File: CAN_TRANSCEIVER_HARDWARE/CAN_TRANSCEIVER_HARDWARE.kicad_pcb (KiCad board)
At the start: 2 copper layers, 143.7 x 76.6 mm, 112 parts, among them J101 5v_pin_terminal, J102 5V Inp, J103 SPI Remaining Pin, J104 SPI 1, J105 SPI Remaining Pin, J106 SPI 3, J107 SPI 2 Remaining Pin, J108 SPI 2, J109 SPI Remaining Pin, J110 SPI 4, J111 UART 1, J112 UART 2, J113 UART 3, J114 UART 4, J115 Screw_Terminal_01x02, J116 Screw_Terminal_01x02, J117 Screw_Terminal_01x02, J118 Screw_Terminal_01x02, J119 Screw_Terminal_01x02, J120 Screw_Terminal_01x02, J121 Screw_Terminal_01x02, J122 Screw_Terminal_01x02, SW101 SW_DIP_x04, SW102 SW_DIP_x04, U101 MCP2515-xSO, U102 MCP2515-xSO, U103 MCP2515-xSO, U104 MCP2515-xSO, U105 MCP25612FD-E/SL, U106 ATA6565-GCQW1, U107 MCP25612FD-E/SL, U108 ATA6565-GCQW1, Y101 Crystal, Y102 Crystal, Y103 Crystal, Y104 Crystal

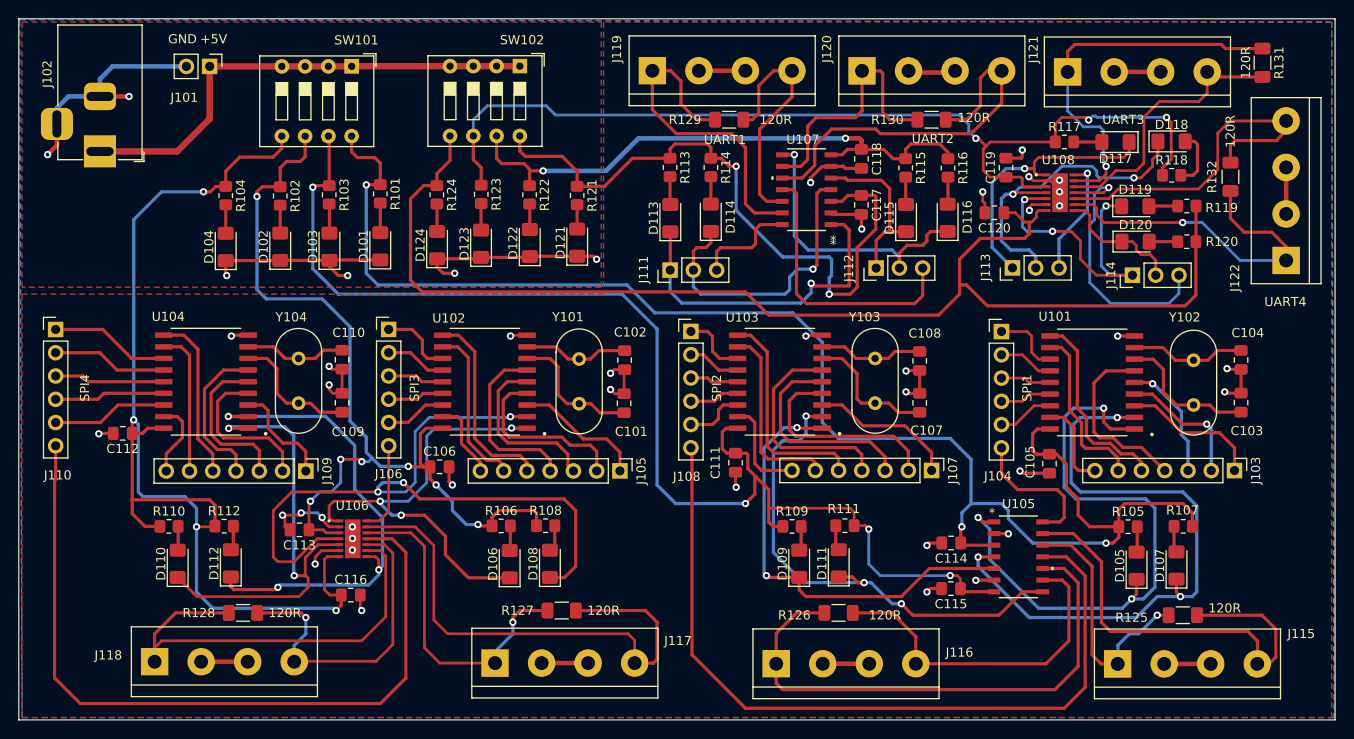
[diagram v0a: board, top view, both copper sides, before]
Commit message: Added logo in the PCB and added stackup table
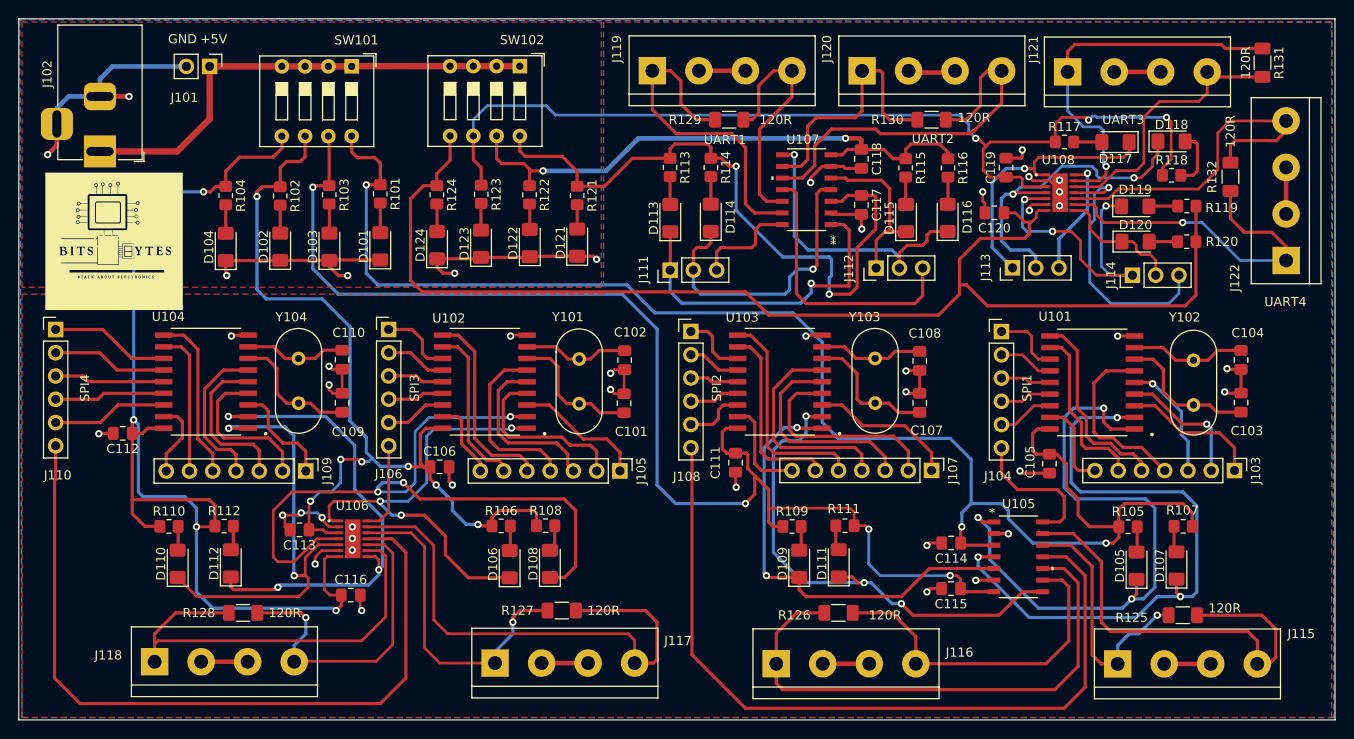
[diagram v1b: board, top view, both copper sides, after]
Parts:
- added G***: LOGO, LOGO, F.Cu at (61.1, 75.0)
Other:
- board text added: "0"
- board text added: "0 mm"
- board text added: "0.0000 mm / 0.0000 mm"
- board text added: "0.01 mm"
- board text added: "0.02"
- board text added: "0.035 mm"
- board text added: "0.3000 mm"
- board text added: "1.51 mm"
- board text added: "1.6000 mm"
- board text added: "143.7200 mm x 76.5556 mm"
- board text added: "3.3"
- board text added: "4.5"
- board text added: "B.Cu"
- board text added: "B.Mask"
- board text added: "B.Paste"
- board text added: "B.Silkscreen"
- board text added: "BOARD CHARACTERISTICS"
- board text added: "Board Thickness:"
- board text added: "Board overall dimensions:"
- board text added: "Bottom Silk Screen"
- board text added: "Bottom Solder Mask"
- board text added: "Bottom Solder Paste"
- board text added: "Castellated pads:"
- board text added: "Color"
- board text added: "Copper Finish:"
- board text added: "Copper Layer Count:"
- board text added: "Dielectric"
- board text added: "Edge card connectors:"
- board text added: "Epsilon R"
- board text added: "F.Cu"
- board text added: "F.Mask"
- board text added: "F.Paste"
- board text added: "F.Silkscreen"
- board text added: "FR4"
- board text added: "Impedance Control:"
- board text added: "Layer Name"
- board text added: "Loss Tangent"
- board text added: "Material"
- board text added: "Min hole diameter:"
- board text added: "Min track/spacing:"
- board text added: "No"
- board text added: "None"
- board text added: "Not specified"
- board text added: "Plated Board Edge:"
- board text added: "Thickness (mm)"
- board text added: "Top Silk Screen"
- board text added: "Top Solder Mask"
- board text added: "Top Solder Paste"
- board text added: "Type"
- board text added: "copper"
- board text added: "core"
